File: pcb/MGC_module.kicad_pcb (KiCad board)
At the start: 2 copper layers, 33 x 48.9 mm, 53 parts, among them J11 103P012BB100, J12 103P012BB100, J13 103P012BB100, J3 103P012BB100, J7 103P012BB100, SW1 SW_DIP_x02, U1 74LVC4066, U2 74AHC1G14, U3 ATmega16A-A, Y1 12MHz

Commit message: Update uart series resistor values
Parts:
- R11, R12: value 0 -> 22k
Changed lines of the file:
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@@
 			)
 		)
-		(property "Value" "0"
-			(at 2.4785 0 90)
+		(property "Value" "22k"
+			(at 3.4945 0 90)
 			(layer "B.Fab")
 			(effects
@@
 			)
 		)
-		(property "Value" "0"
-			(at -2.413 0 0)
-			(layer "B.Fab")
-			(effects
+		(property "Value" "22k"
+			(at -0.0254 1.8796 0)
+			(layer "B.Fab")
+			(effects

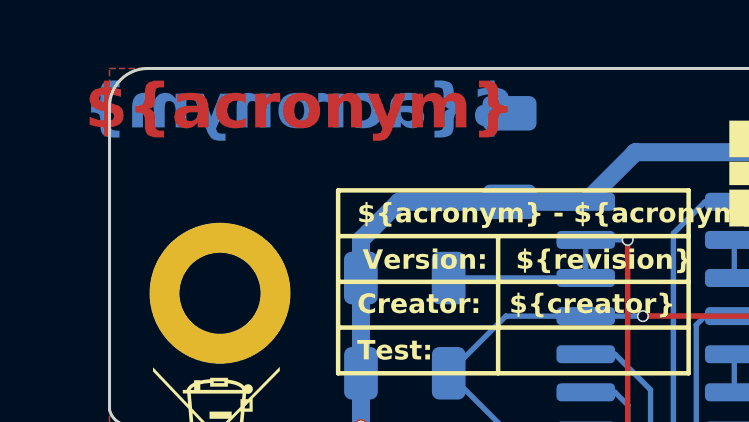
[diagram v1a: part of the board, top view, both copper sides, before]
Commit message: Decrease font size of cu acronym
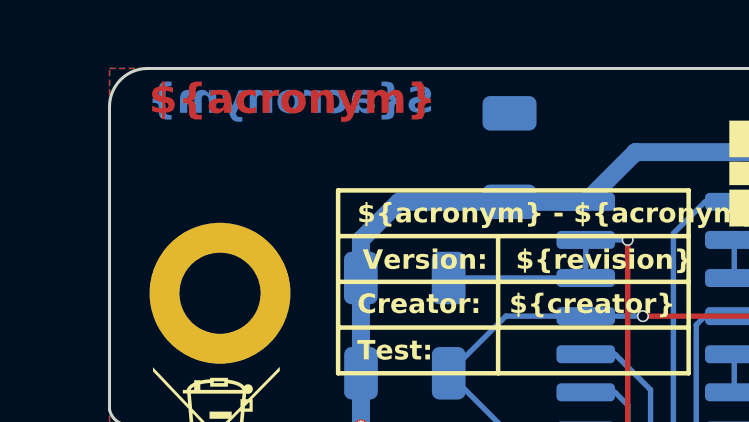
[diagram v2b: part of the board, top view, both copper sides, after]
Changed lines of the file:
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@@
 	)
 	(gr_text "${acronym}\n"
-		(at 139.7 64.770001 0)
+		(at 139.446 64.516001 0)
 		(layer "F.Cu")
 		(effects
 			(font
-				(size 1.5 1.5)
-				(thickness 0.3)
+				(size 1 1)
+				(thickness 0.2)
 				(bold yes)
 			)
@@
 	)
 	(gr_text "${acronym}\n"
-		(at 139.6492 64.770001 0)
+		(at 139.3952 64.516001 0)
 		(layer "B.Cu")
 		(effects
 			(font
-				(size 1.5 1.5)
-				(thickness 0.3)
+				(size 1 1)
+				(thickness 0.2)
 				(bold yes)
 			)
@@
 		(layer "Dwgs.User")
 		(pts
-			(xy 133.35 63.500001) (xy 167.64 63.500001)
+			(xy 133.35 63.500001) (xy 166.37 63.500001)
 		)
 		(height -3.81)
@@
 			(keep_text_aligned yes)
 		)
-		(gr_text "34.29"
-			(at 150.495 58.540001 0)
+		(gr_text "33.02"
+			(at 149.86 58.540001 0)
 			(layer "Dwgs.User")
 			(effects
@@
 			)
 		)
-	)
-	(zone
-		(net 0)
-		(net_name "")
-		(layers "F.Cu" "B.Cu")
-		(hatch edge 0.5)
-		(connect_pads
-			(clearance 0)
-		)
-		(min_thickness 0.25)
-		(filled_areas_thickness no)
-		(keepout
-			(tracks allowed)
-			(vias allowed)
-			(pads allowed)
-			(copperpour not_allowed)
-			(footprints allowed)
-		)
-		(placement
-			(enabled no)
-			(sheetname "")
-		)
-		(fill
-			(thermal_gap 0.5)
-			(thermal_bridge_width 0.5)
-		)
-		(polygon
-			(pts
-				(xy 133.7564 65.887601) (xy 133.2484 65.887601) (xy 133.2484 65.786001) (xy 133.7564 65.786001)
-			)
-		)

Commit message: Adapt VDD traces
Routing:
- net VDD: track 146.7 -> 144.6 mm
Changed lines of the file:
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@@
+	)
+	(segment
+		(start 162.433 73.025001)
+		(end 163.266 73.025001)
+		(width 0.4)
+		(layer "F.Cu")
+		(net 6)
+	)
+	(segment
+		(start 163.266 74.168001)
+		(end 163.266 73.025001)
+		(width 0.4)
+		(layer "F.Cu")
+		(net 6)
+	)
+	(segment
+		(start 162.616 102.235001)
+		(end 162.616 102.870001)
+		(width 0.4)
+		(layer "F.Cu")
+		(net 6)
 	)
 	(segment
@@
 	)
 	(segment
-		(start 162.433 73.025001)
-		(end 163.266 73.025001)
-		(width 0.4)
-		(layer "F.Cu")
-		(net 6)
-	)
-	(segment
-		(start 163.266 74.168001)
-		(end 163.266 73.025001)
-		(width 0.4)
-		(layer "F.Cu")
-		(net 6)
-	)
-	(segment
-		(start 138.432998 82.042001)
-		(end 136.85 83.624999)
-		(width 0.4)
-		(layer "F.Cu")
-		(net 6)
-	)
-	(segment
-		(start 162.616 102.235001)
-		(end 162.616 102.870001)
-		(width 0.4)
-		(layer "F.Cu")
-		(net 6)
-	)
-	(segment
-		(start 147.574 82.042001)
-		(end 138.432998 82.042001)
-		(width 0.4)
-		(layer "F.Cu")
-		(net 6)
-	)
-	(segment
 		(start 136.85 83.624999)
 		(end 136.2 83.624999)
@@
 	)
 	(segment
+		(start 138.432998 82.042001)
+		(end 138.304499 82.1705)
+		(width 0.4)
+		(layer "F.Cu")
+		(net 6)
+	)
+	(segment
 		(start 151.892 94.869001)
 		(end 151.892 100.203001)
+		(width 0.4)
+		(layer "F.Cu")
+		(net 6)
+	)
+	(segment
+		(start 148.209 86.423001)
+		(end 148.209 82.677001)
+		(width 0.4)
+		(layer "F.Cu")
+		(net 6)
+	)
+	(segment
+		(start 163.266 75.116001)
+		(end 163.266 74.168001)
 		(width 0.4)
 		(layer "F.Cu")
@@
 	)
 	(segment
-		(start 163.266 75.116001)
-		(end 163.266 74.168001)
-		(width 0.4)
-		(layer "F.Cu")
-		(net 6)
-	)
-	(segment
-		(start 148.209 86.423001)
-		(end 148.209 82.677001)
+		(start 136.2 101.404999)
+		(end 136.85 101.404999)
 		(width 0.4)
 		(layer "F.Cu")
@@
 		(start 162.616 102.870001)
 		(end 162.616 104.198999)
+		(width 0.4)
+		(layer "F.Cu")
+		(net 6)
+	)
+	(segment
+		(start 147.574 82.042001)
+		(end 138.432998 82.042001)
 		(width 0.4)
 		(layer "F.Cu")
@@
 	)
 	(segment
+		(start 151.861499 94.8385)
+		(end 151.892 94.869001)
+		(width 0.4)
+		(layer "F.Cu")
+		(net 6)
+	)
+	(segment
+		(start 163.266 104.198999)
+		(end 162.616 104.198999)
+		(width 0.4)
+		(layer "F.Cu")
+		(net 6)
+	)
+	(segment
+		(start 162.616 75.116001)
+		(end 163.266 75.116001)
+		(width 0.4)
+		(layer "F.Cu")
+		(net 6)
+	)
+	(segment
+		(start 136.2 90.228999)
+		(end 136.85 90.228999)
+		(width 0.4)
+		(layer "F.Cu")
+		(net 6)
+	)
+	(segment
 		(start 141.732 78.742999)
 		(end 136.85 83.624999)
@@
 		(net 6)
 	)
-	(segment
-		(start 151.861499 94.8385)
-		(end 151.892 94.869001)
-		(width 0.4)
-		(layer "F.Cu")
-		(net 6)
-	)
-	(segment
-		(start 163.266 104.198999)
-		(end 162.616 104.198999)
-		(width 0.4)
-		(layer "F.Cu")
-		(net 6)
-	)
-	(segment
-		(start 162.616 75.116001)
-		(end 163.266 75.116001)
-		(width 0.4)
-		(layer "F.Cu")
-		(net 6)
-	)
-	(segment
-		(start 136.2 90.228999)
-		(end 136.85 90.228999)
-		(width 0.4)
-		(layer "F.Cu")
-		(net 6)
-	)
-	(segment
-		(start 136.2 101.404999)
-		(end 136.85 101.404999)
-		(width 0.4)
-		(layer "F.Cu")
-		(net 6)
-	)
 	(via
 		(at 162.616 102.870001)
@@
 	)
 	(segment
-		(start 148.6425 97.320001)
-		(end 146.05 97.320001)
-		(width 0.4)
-		(layer "B.Cu")
-		(net 6)
-	)
-	(segment
 		(start 154.305 88.265001)
 		(end 162.56 88.265001)
@@
 		(layer "B.Cu")
 		(net 6)
+	)
+	(segment
+		(start 148.6425 97.320001)
+		(end 146.05 97.320001)
+		(width 0.4)
+		(layer "B.Cu")
+		(net 6)
